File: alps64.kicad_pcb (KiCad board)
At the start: 2 copper layers, 285 x 95.2 mm, 200 parts, among them J1 USB_mini_micro_B, K00 KEYSW, K00_1 KEYSW, K00_2 KEYSW, K00_3 KEYSW, K01 KEYSW, K02 KEYSW, K03 KEYSW, K04 KEYSW, K05 KEYSW, K06 KEYSW, K07 KEYSW, K10 KEYSW, K10_1 KEYSW, K10_2 KEYSW, K11 KEYSW, K12 KEYSW, K13 KEYSW, K14 KEYSW, K15 KEYSW, K16 KEYSW, K17 KEYSW, K20 KEYSW, K20_1 KEYSW, K21 KEYSW, K21_1 KEYSW, K22 KEYSW, K23 KEYSW, K23_1 KEYSW, K23_2 KEYSW, K23_3 KEYSW, K24 KEYSW, K24_1 KEYSW, K25 KEYSW, K26 KEYSW, K27 KEYSW, K27_1 KEYSW, K30 KEYSW, K30_1 KEYSW, K31 KEYSW, K31_1 KEYSW, K32 KEYSW, K32_1 KEYSW, K32_2 ALPS_SKCM, K33 KEYSW, K34 KEYSW, K35 KEYSW, K36 KEYSW, K37 KEYSW, K40 KEYSW, K40_1 KEYSW, K40_2 KEYSW, K41 KEYSW, K42 KEYSW, K43 KEYSW, K44 KEYSW, K45 KEYSW, K46 KEYSW, K47 KEYSW, K50 KEYSW, K50_1 KEYSW, K50_2 KEYSW, K51 KEYSW, K52 KEYSW, K53 KEYSW, K54 KEYSW, K55 KEYSW, K56 KEYSW, K57 KEYSW, K60 KEYSW, K60_1 KEYSW, K60_2 KEYSW, K61 KEYSW, K62 KEYSW, K63 KEYSW, K64 KEYSW, K65 KEYSW, K66 KEYSW, K67 KEYSW, K70 KEYSW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

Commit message: Save the project files using Kicad 7
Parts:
- removed G***: LOGO, keyboard_parts:tmk_logo
- removed K32_2: ALPS_SKCM, keyboard_parts:ALPS_SKCM
- removed P?: GND, keyboard_parts:PIN_1
- removed P?: 5V, keyboard_parts:PIN_1
- removed P?: C6, keyboard_parts:PIN_1
- removed P?: C4, keyboard_parts:PIN_1
- removed P?: C7, keyboard_parts:PIN_1
- removed the Poker_oval_hole at (128.7, 33.3)
- removed the Poker_oval_hole at (195.4, 90.5)
- removed the Poker_oval_hole at (265.1, 90.5)
- removed the Poker_oval_hole at (30.1, 90.5)
- removed the Poker_oval_hole at (166.7, 33.3)
- removed the Poker_oval_hole at (152.4, 52.4)
- removed Poker_side_edge_long (x2): VAL**, keyboard_parts:Poker_side_edge_long
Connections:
- net /matrix/col5 renamed /col5
- net /matrix/col7 renamed /col7
- net /matrix/row4 renamed /row4
- C3 pad 1: Net-(C3-Pad1) -> Net-(U1-XTAL2)
- C4 pad 1: Net-(C4-Pad1) -> Net-(U1-XTAL1)
- D01 pad 2: /matrix/row0 -> /row0
- D02 pad 2: /matrix/row0 -> /row0
- D03 pad 2: /matrix/row0 -> /row0
- D04 pad 2: /matrix/row0 -> /row0
- D05 pad 2: /matrix/row0 -> /row0
- D06 pad 2: /matrix/row0 -> /row0
- D07 pad 2: /matrix/row0 -> /row0
- D11 pad 2: /matrix/row1 -> /row1
- D12 pad 2: /matrix/row1 -> /row1
- D13 pad 2: /matrix/row1 -> /row1
- D14 pad 2: /matrix/row1 -> /row1
- D15 pad 2: /matrix/row1 -> /row1
- D16 pad 2: /matrix/row1 -> /row1
- D17 pad 2: /matrix/row1 -> /row1
- D21 pad 2: /matrix/row2 -> /row2
- D32 pad 2: /matrix/row3 -> /row3
- D33 pad 2: /matrix/row3 -> /row3
- D34 pad 2: /matrix/row3 -> /row3
- D35 pad 2: /matrix/row3 -> /row3
- D37 pad 2: /matrix/row3 -> /row3
- D50 pad 2: /matrix/row5 -> /row5
- D51 pad 2: /matrix/row5 -> /row5
- D52 pad 2: /matrix/row5 -> /row5
- D53 pad 2: /matrix/row5 -> /row5
- D54 pad 2: /matrix/row5 -> /row5
- D56 pad 2: /matrix/row5 -> /row5
- D57 pad 2: /matrix/row5 -> /row5
- D60 pad 2: /matrix/row6 -> /row6
- D61 pad 2: /matrix/row6 -> /row6
- D62 pad 2: /matrix/row6 -> /row6
- D64 pad 2: /matrix/row6 -> /row6
- D66 pad 2: /matrix/row6 -> /row6
- D67 pad 2: /matrix/row6 -> /row6
- D71 pad 2: /matrix/row7 -> /row7
- D72 pad 2: /matrix/row7 -> /row7
- D74 pad 2: /matrix/row7 -> /row7
- D75 pad 2: /matrix/row7 -> /row7
- D76 pad 2: /matrix/row7 -> /row7
- D77 pad 2: /matrix/row7 -> /row7
- K00_2 pad 1: /matrix/col0 -> /col0
- K01 pad 1: /matrix/col1 -> /col1
- K02 pad 1: /matrix/col2 -> /col2
- K03 pad 1: /matrix/col3 -> /col3
- K04 pad 1: /matrix/col4 -> /col4
- K06 pad 1: /matrix/col6 -> /col6
- K10_2 pad 1: /matrix/col0 -> /col0
- K11 pad 1: /matrix/col1 -> /col1
- K12 pad 1: /matrix/col2 -> /col2
- K13 pad 1: /matrix/col3 -> /col3
- K14 pad 1: /matrix/col4 -> /col4
- K16 pad 1: /matrix/col6 -> /col6
- K20_1 pad 1: /matrix/col0 -> /col0
- K21_1 pad 1: /matrix/col1 -> /col1
- K22 pad 1: /matrix/col2 -> /col2
- K23 pad 1: /matrix/col3 -> /col3
- K23_1 pad 1: /matrix/col3 -> /col3
- K26 pad 1: /matrix/col6 -> /col6
- K30_1 pad 1: /matrix/col0 -> /col0
- K31_1 pad 1: /matrix/col1 -> /col1
- K32_1 pad 1: /matrix/col2 -> /col2
- K33 pad 1: /matrix/col3 -> /col3
- K34 pad 1: /matrix/col4 -> /col4
- K40_1 pad 1: /matrix/col0 -> /col0
- K40_2 pad 1: /matrix/col0 -> /col0
- K42 pad 1: /matrix/col2 -> /col2
- K43 pad 1: /matrix/col3 -> /col3
- K44 pad 1: /matrix/col4 -> /col4
- K46 pad 1: /matrix/col6 -> /col6
- K50_1 pad 1: /matrix/col0 -> /col0
- K51 pad 1: /matrix/col1 -> /col1
- K52 pad 1: /matrix/col2 -> /col2
- K53 pad 1: /matrix/col3 -> /col3
- K54 pad 1: /matrix/col4 -> /col4
- K56 pad 1: /matrix/col6 -> /col6
- K60_2 pad 1: /matrix/col0 -> /col0
- K61 pad 1: /matrix/col1 -> /col1
- K62 pad 1: /matrix/col2 -> /col2
- K63 pad 1: /matrix/col3 -> /col3
- K64 pad 1: /matrix/col4 -> /col4
- K66 pad 1: /matrix/col6 -> /col6
- K70_1 pad 1: /matrix/col0 -> /col0
- K71 pad 1: /matrix/col1 -> /col1
- K72 pad 1: /matrix/col2 -> /col2
- K73 pad 1: /matrix/col3 -> /col3
- K74 pad 1: /matrix/col4 -> /col4
- K76 pad 1: /matrix/col6 -> /col6
- R4 pad 1: Net-(LED1-Pad2) -> Net-(LED1-A)
- U1 pad 1: Net-(C4-Pad1) -> Net-(U1-XTAL1)
- U1 pad 11: /matrix/row5 -> /row5
- U1 pad 12: /matrix/row6 -> /row6
- U1 pad 14: /matrix/col0 -> /col0
- U1 pad 15: /matrix/col1 -> /col1
- U1 pad 16: /matrix/col2 -> /col2
- U1 pad 17: /matrix/col3 -> /col3
- U1 pad 18: /matrix/col4 -> /col4
- U1 pad 2: Net-(C3-Pad1) -> Net-(U1-XTAL2)
- U1 pad 20: /matrix/col6 -> /col6
- U1 pad 22: Net-(U1-Pad22) -> unconnected-(U1-PC7-Pad22)
- U1 pad 23: Net-(U1-Pad23) -> unconnected-(U1-PC6-Pad23)
- U1 pad 25: Net-(LED1-Pad1) -> Net-(LED1-K)
- U1 pad 26: Net-(U1-Pad26) -> unconnected-(U1-PC4-Pad26)
- U1 pad 5: /matrix/row7 -> /row7
- U1 pad 6: /matrix/row0 -> /row0
- U1 pad 7: /matrix/row1 -> /row1
- U1 pad 8: /matrix/row2 -> /row2
- U1 pad 9: /matrix/row3 -> /row3
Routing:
- net unconnected-(U1-PC4-Pad26): track 0.00 -> 25.3 mm, vias 0 -> 1
- net Net-(U1-Pad26): track 25.3 -> 0.00 mm, vias 1 -> 0
- net Net-(U1-Pad23): track 17.5 -> 0.00 mm, vias 1 -> 0
- net unconnected-(U1-PC6-Pad23): track 0.00 -> 17.5 mm, vias 0 -> 1
- net Net-(U1-Pad22): track 14.0 -> 0.00 mm, vias 1 -> 0
- net unconnected-(U1-PC7-Pad22): track 0.00 -> 14.0 mm, vias 0 -> 1
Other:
- net class 20mil removed
- net class 6mil removed
- net class 8mil removed
- net class Default removed
- net class Power removed

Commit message: Update footprints
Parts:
- removed D00, D10, D20, D22, D23, D24, D25, D26, D27, D30, D31, D36, D55, D63, D65, D70, D73: D, keyboard_parts:D_axial
- removed D00, D10, D20, D22, D23, D24, D25, D26, D27, D30, D31, D36, D55, D63, D65, D70, D73: D, keyboard_parts:D_SOD123_hand
- removed D01, D02, D03, D04, D05, D06, D07, D11, D12, D13, D14, D15, D16, D17, D21, D32, D33, D34, D35, D37, D40, D41, D42, D43, D44, D45, D46, D47, D50, D51, D52, D53, D54, D56, D57, D60, D61, D62, D64, D66, D67, D71, D72, D74, D75, D76, D77: D, keyboard_parts:D_SOD123_axial
- removed J1: USB_mini_micro_B, keyboard_parts:USB_miniB_hirose_5S8
- removed K00, K00_1, K00_3, K10, K10_1, K20, K21, K24, K24_1, K30, K31, K32, K36, K40, K41, K50, K50_2, K60, K60_1, K70: KEYSW, keyboard_parts:ALPS_SKCM_reverse_pad
- removed K00_2, K01, K02, K03, K04, K05, K06, K07, K10_2, K11, K12, K13, K14, K15, K16, K17, K20_1, K21_1, K22, K23, K23_1, K23_2, K23_3, K25, K26, K27, K27_1, K30_1, K31_1, K32_1, K33, K34, K35, K37, K40_1, K40_2, K42, K43, K44, K45, K46, K47, K50_1, K51, K52, K53, K54, K55, K56, K57, K60_2, K61, K62, K63, K64, K65, K66, K67, K70_1, K71, K72, K73, K74, K75, K76, K77: KEYSW, keyboard_parts:ALPS_SKCM
- removed Poker_oval_hole (x3): VAL**, keyboard_parts:Poker_oval_hole
- added D18: D, Diode_SMD:D_SOD-323, F.Cu at (120.9, 121.3)
- added D19: D, Diode_SMD:D_SOD-323, F.Cu at (120.9, 125.6)
- added D28: D, Diode_SMD:D_SOD-323, F.Cu at (120.9, 129.8)
- added D29: D, Diode_SMD:D_SOD-323, F.Cu at (120.9, 134.1)
- added D8: D, Diode_SMD:D_SOD-323, F.Cu at (120.9, 112.8)
- added D9: D, Diode_SMD:D_SOD-323, F.Cu at (120.9, 117.1)
- added J2: USB_C_Receptacle, Connector_USB:USB_C_Receptacle_HCTL_HC-TYPE-C-16P-01A, F.Cu at (76.8, 86.1)
- added K18: keyboard_parts:KEYSW, Button_Switch_Keyboard:SW_Cherry_MX_1.00u_PCB, F.Cu at (152.1, 75.3)
- added K19: keyboard_parts:KEYSW, Button_Switch_Keyboard:SW_Cherry_MX_1.00u_PCB, F.Cu at (152.1, 95.5)
- added K28: keyboard_parts:KEYSW, Button_Switch_Keyboard:SW_Cherry_MX_1.00u_PCB, F.Cu at (172.3, 75.3)
- added K29: keyboard_parts:KEYSW, Button_Switch_Keyboard:SW_Cherry_MX_1.00u_PCB, F.Cu at (172.3, 95.5)
- added K8: keyboard_parts:KEYSW, Button_Switch_Keyboard:SW_Cherry_MX_1.00u_PCB, F.Cu at (131.9, 75.3)
- added K9: keyboard_parts:KEYSW, Button_Switch_Keyboard:SW_Cherry_MX_1.00u_PCB, F.Cu at (131.9, 95.5)
- C1: footprint keyboard_parts:C_3216 -> Capacitor_SMD:C_0603_1608Metric; moved to F.Cu
- C2, C3, C4: footprint keyboard_parts:C_1608 -> Capacitor_SMD:C_0603_1608Metric; moved to F.Cu
- C5, C6: footprint keyboard_parts:C_1608 -> Capacitor_THT:C_Disc_D3.0mm_W1.6mm_P2.50mm; moved to F.Cu
- LED1: footprint keyboard_parts:LED_3020_REFLOW -> LED_THT:LED_D1.8mm_W3.3mm_H2.4mm; moved to F.Cu
- R1, R2, R3, R4: footprint keyboard_parts:R_1608 -> Resistor_THT:R_Axial_DIN0204_L3.6mm_D1.6mm_P7.62mm_Horizontal; moved to F.Cu
- SW100: footprint keyboard_parts:SW_ALPS_SKRP -> Button_Switch_THT:SW_PUSH_6mm; moved to F.Cu
- U1: footprint keyboard_parts:QFP32_reflow -> Package_QFP:TQFP-32_7x7mm_P0.8mm; moved to F.Cu
- X1: value CRYSTAL -> 16MHz; footprint keyboard_parts:FA-238 -> Crystal:Crystal_SMD_3225-4Pin_3.2x2.5mm; moved to F.Cu
- moved LED1 79.0 mm to (90.8, 105.3)
- moved R4 78.7 mm to (90.6, 101.7)
- moved U1 53.6 mm to (54.5, 88.8), turned to 0 degrees
- moved SW100 45.9 mm to (50.7, 96.7)
- moved X1 43.4 mm to (85.0, 111.2)
- moved C4 41.1 mm to (85.0, 101.7)
- moved C3 39.3 mm to (85.0, 98.5)
- moved C6 38.1 mm to (85.0, 108.0)
- moved C5 34.5 mm to (85.0, 104.8)
- moved C2 29.7 mm to (85.0, 95.4), turned to 0 degrees
- moved R1 26.4 mm to (90.6, 92.2), turned to 0 degrees
- moved R2 26.4 mm to (90.6, 95.4), turned to 0 degrees
- moved C1 19.5 mm to (85.0, 92.2), turned to 0 degrees
- moved R3 8.34 mm to (90.6, 98.5), turned to 0 degrees
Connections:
- LED1 pad 1: Net-(LED1-Pad2) -> Net-(LED1-K)
- LED1 pad 2: Net-(LED1-Pad1) -> Net-(LED1-A)
- U1 pad 10: /row4 -> unconnected-(U1-PD4-Pad10)
- U1 pad 11: /row5 -> unconnected-(U1-PD5-Pad11)
- U1 pad 12: /row6 -> unconnected-(U1-PD6-Pad12)
- U1 pad 14: /col0 -> /COL0
- U1 pad 15: /col1 -> /COL1
- U1 pad 16: /col2 -> unconnected-(U1-PB2-Pad16)
- U1 pad 17: /col3 -> unconnected-(U1-PB3-Pad17)
- U1 pad 18: /col4 -> unconnected-(U1-PB4-Pad18)
- U1 pad 19: /col5 -> unconnected-(U1-PB5-Pad19)
- U1 pad 20: /col6 -> unconnected-(U1-PB6-Pad20)
- U1 pad 21: /col7 -> unconnected-(U1-PB7-Pad21)
- U1 pad 5: /row7 -> unconnected-(U1-PC2-Pad5)
- U1 pad 6: /row0 -> /ROW0
- U1 pad 7: /row1 -> /ROW1
- U1 pad 8: /row2 -> /ROW2
- U1 pad 9: /row3 -> unconnected-(U1-PD3/TXD1-Pad9)
- X1 pad 1: Net-(C4-Pad1) -> Net-(U1-XTAL1)
- X1 pad 2: Net-(C3-Pad1) -> Net-(U1-XTAL2)
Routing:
- net /matrix/col6: track 448.5 -> 0.00 mm
- net /col7: track 444.8 -> 0.00 mm, vias 1 -> 0
- net /matrix/col4: track 441.9 -> 0.00 mm
- net /matrix/col0: track 436.1 -> 0.00 mm
- net /matrix/col2: track 431.3 -> 0.00 mm
- net /matrix/row2: track 419.6 -> 0.00 mm, vias 1 -> 0
- net /matrix/col3: track 398.1 -> 0.00 mm, vias 1 -> 0
- net /matrix/col1: track 391.0 -> 0.00 mm
- net /col5: track 376.9 -> 0.00 mm, vias 1 -> 0
- net GND: track 337.9 -> 0.00 mm, vias 38 -> 0
- net /matrix/row3: track 311.2 -> 0.00 mm, vias 1 -> 0
- net /matrix/row1: track 295.6 -> 0.00 mm, vias 1 -> 0
- net /matrix/row7: track 277.3 -> 0.00 mm, vias 1 -> 0
- net /matrix/row0: track 270.8 -> 0.00 mm, vias 1 -> 0
- net /matrix/row6: track 245.7 -> 0.00 mm, vias 1 -> 0
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- removed copper zone on B.Cu, net GND
- removed copper zone on F.Cu, net GND
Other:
- board size 285 x 95.2 mm -> 152.1 x 83.7 mm
- board text removed: "K23"
- board text removed: "K24"
- board text removed: "TMK Alps64 Rev.H"
- board text removed: "tmk-kbd.com"

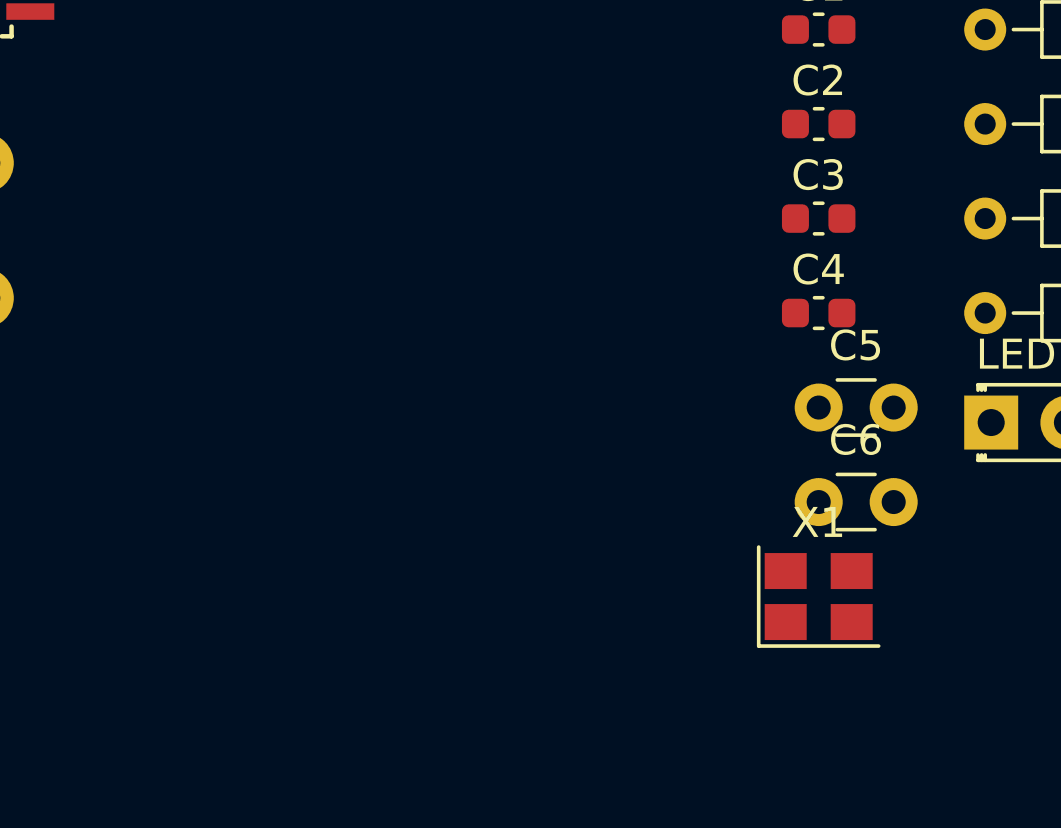
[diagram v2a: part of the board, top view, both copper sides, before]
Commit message: Update footprints
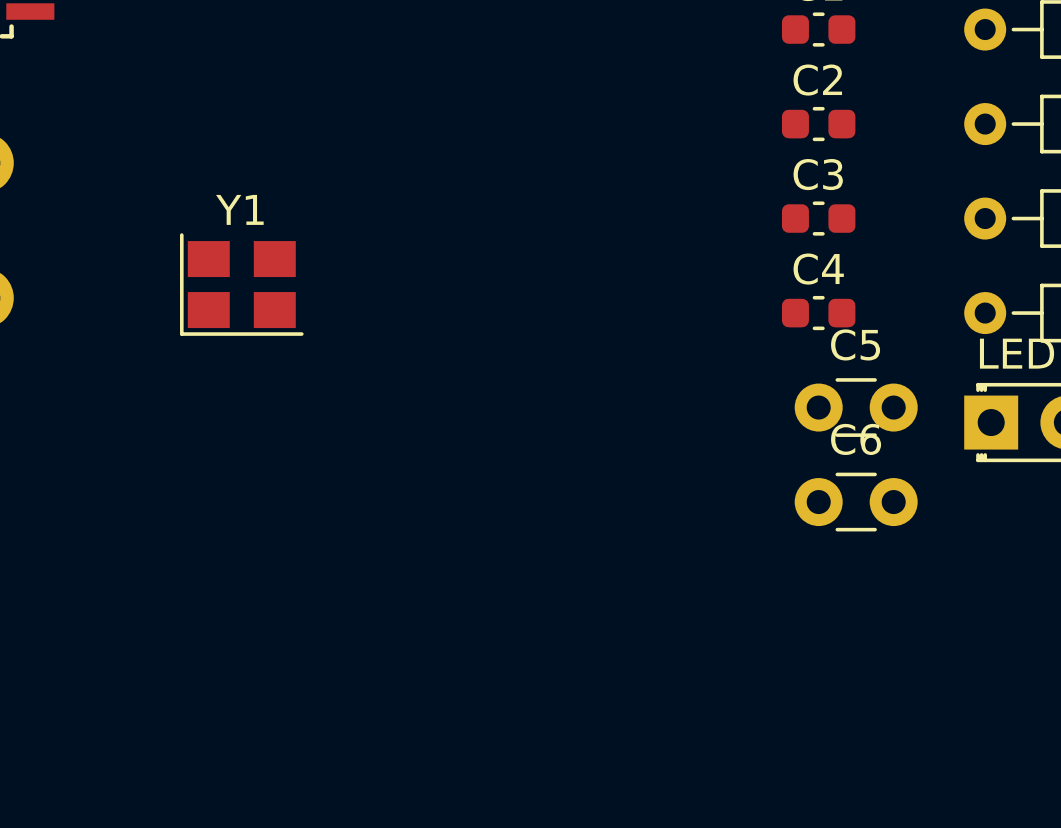
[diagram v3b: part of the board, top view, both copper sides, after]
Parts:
- removed X1: 16MHz, Crystal:Crystal_SMD_3225-4Pin_3.2x2.5mm
- added Y1: Crystal_GND24, Crystal:Crystal_SMD_3225-4Pin_3.2x2.5mm, F.Cu at (65.8, 100.8)
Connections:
- J2 pad A1: Net-(J2-GND-PadA1) -> GND
- J2 pad A12: Net-(J2-GND-PadA1) -> GND
- J2 pad A4: Net-(J2-VBUS-PadA4) -> +5V
- J2 pad A6: unconnected-(J2-D+-PadA6) -> /D+
- J2 pad A7: unconnected-(J2-D--PadA7) -> /D-
- J2 pad A9: Net-(J2-VBUS-PadA4) -> +5V
- J2 pad B1: Net-(J2-GND-PadA1) -> GND
- J2 pad B12: Net-(J2-GND-PadA1) -> GND
- J2 pad B4: Net-(J2-VBUS-PadA4) -> +5V
- J2 pad B6: unconnected-(J2-D+-PadB6) -> /D+
- J2 pad B7: unconnected-(J2-D--PadB7) -> /D-
- J2 pad B9: Net-(J2-VBUS-PadA4) -> +5V
- J2 pad S1: unconnected-(J2-SHIELD-PadS1) -> /SHILED

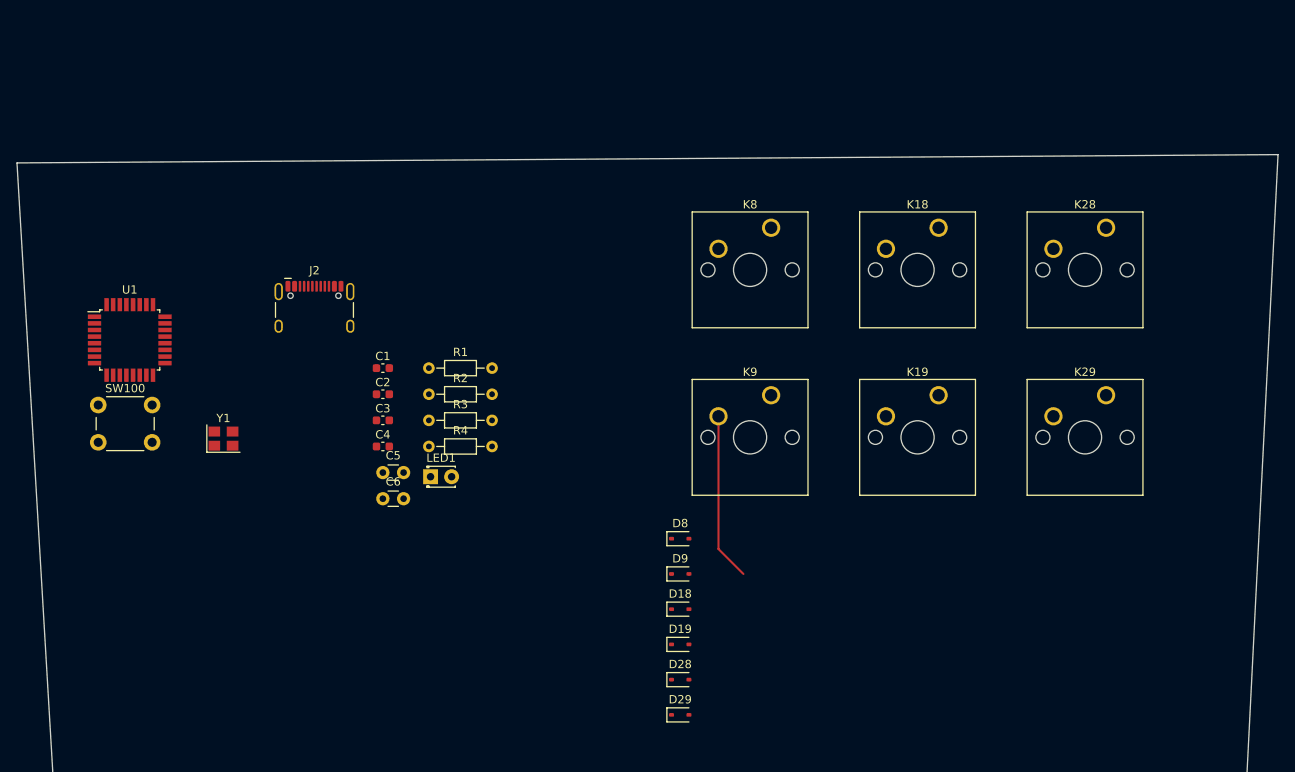
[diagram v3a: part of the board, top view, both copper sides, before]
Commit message: Update parts footprint
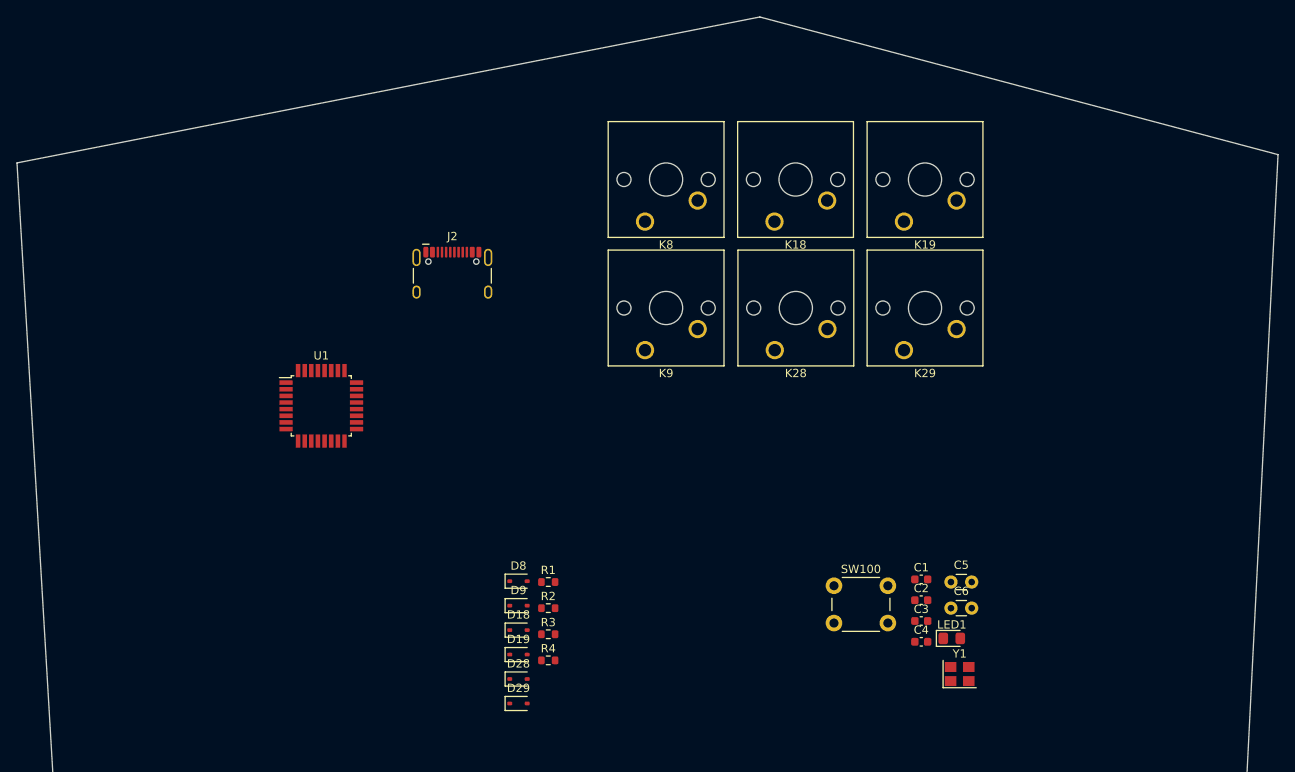
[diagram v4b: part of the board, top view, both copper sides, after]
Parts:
- LED1: footprint LED_THT:LED_D1.8mm_W3.3mm_H2.4mm -> LED_SMD:LED_0805_2012Metric_Pad1.15x1.40mm_HandSolder
- R1, R2, R3, R4: footprint Resistor_THT:R_Axial_DIN0204_L3.6mm_D1.6mm_P7.62mm_Horizontal -> Resistor_SMD:R_0603_1608Metric
- moved Y1 93.2 mm to (154.6, 129.2)
- moved SW100 91.4 mm to (139.4, 118.5)
- moved C5 69.8 mm to (153.6, 118.0)
- moved C6 69.8 mm to (153.6, 121.2)
- moved C1 69.8 mm to (150.0, 117.7)
- moved C2 69.5 mm to (150.0, 120.2)
- moved C3 69.3 mm to (150.0, 122.8)
- moved C4 69.1 mm to (150.0, 125.3)
- moved LED1 65.8 mm to (153.7, 124.8)
- moved K28 42.6 mm to (132.3, 90.1), turned to 180 degrees
- moved R1 29.5 mm to (105.0, 118.0)
- moved R2 29.5 mm to (105.0, 121.2)
- moved R3 29.5 mm to (105.0, 124.3)
- moved R4 29.5 mm to (105.0, 127.5)
- moved K29 25.0 mm to (147.9, 90.1), turned to 180 degrees
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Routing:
- net Net-(D9-A): track 20.3 -> 0.00 mm
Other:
- board size 152.1 x 83.7 mm -> 152.1 x 100.3 mm
